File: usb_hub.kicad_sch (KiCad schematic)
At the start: 89 parts, among them J5 USB-C_WE_632723300011, J6 USB-C_WE_632723300011, U16 AP7366_SOT, U17 TPD4E05U06QDQARQ1, U18 AP22615A_TSOT26, U19 TPD4E05U06QDQARQ1, U20 AP22615A_TSOT26, U21 USB7252C, U22 W25Q80DV_USON, U24 TPD4E05U06QDQARQ1, U25 TPD4E05U06QDQARQ1, U27 TPD4E05U06QDQARQ1, U28 TPD4E05U06QDQARQ1, Y2 Oscillator_25MHz_ESC_2016MV

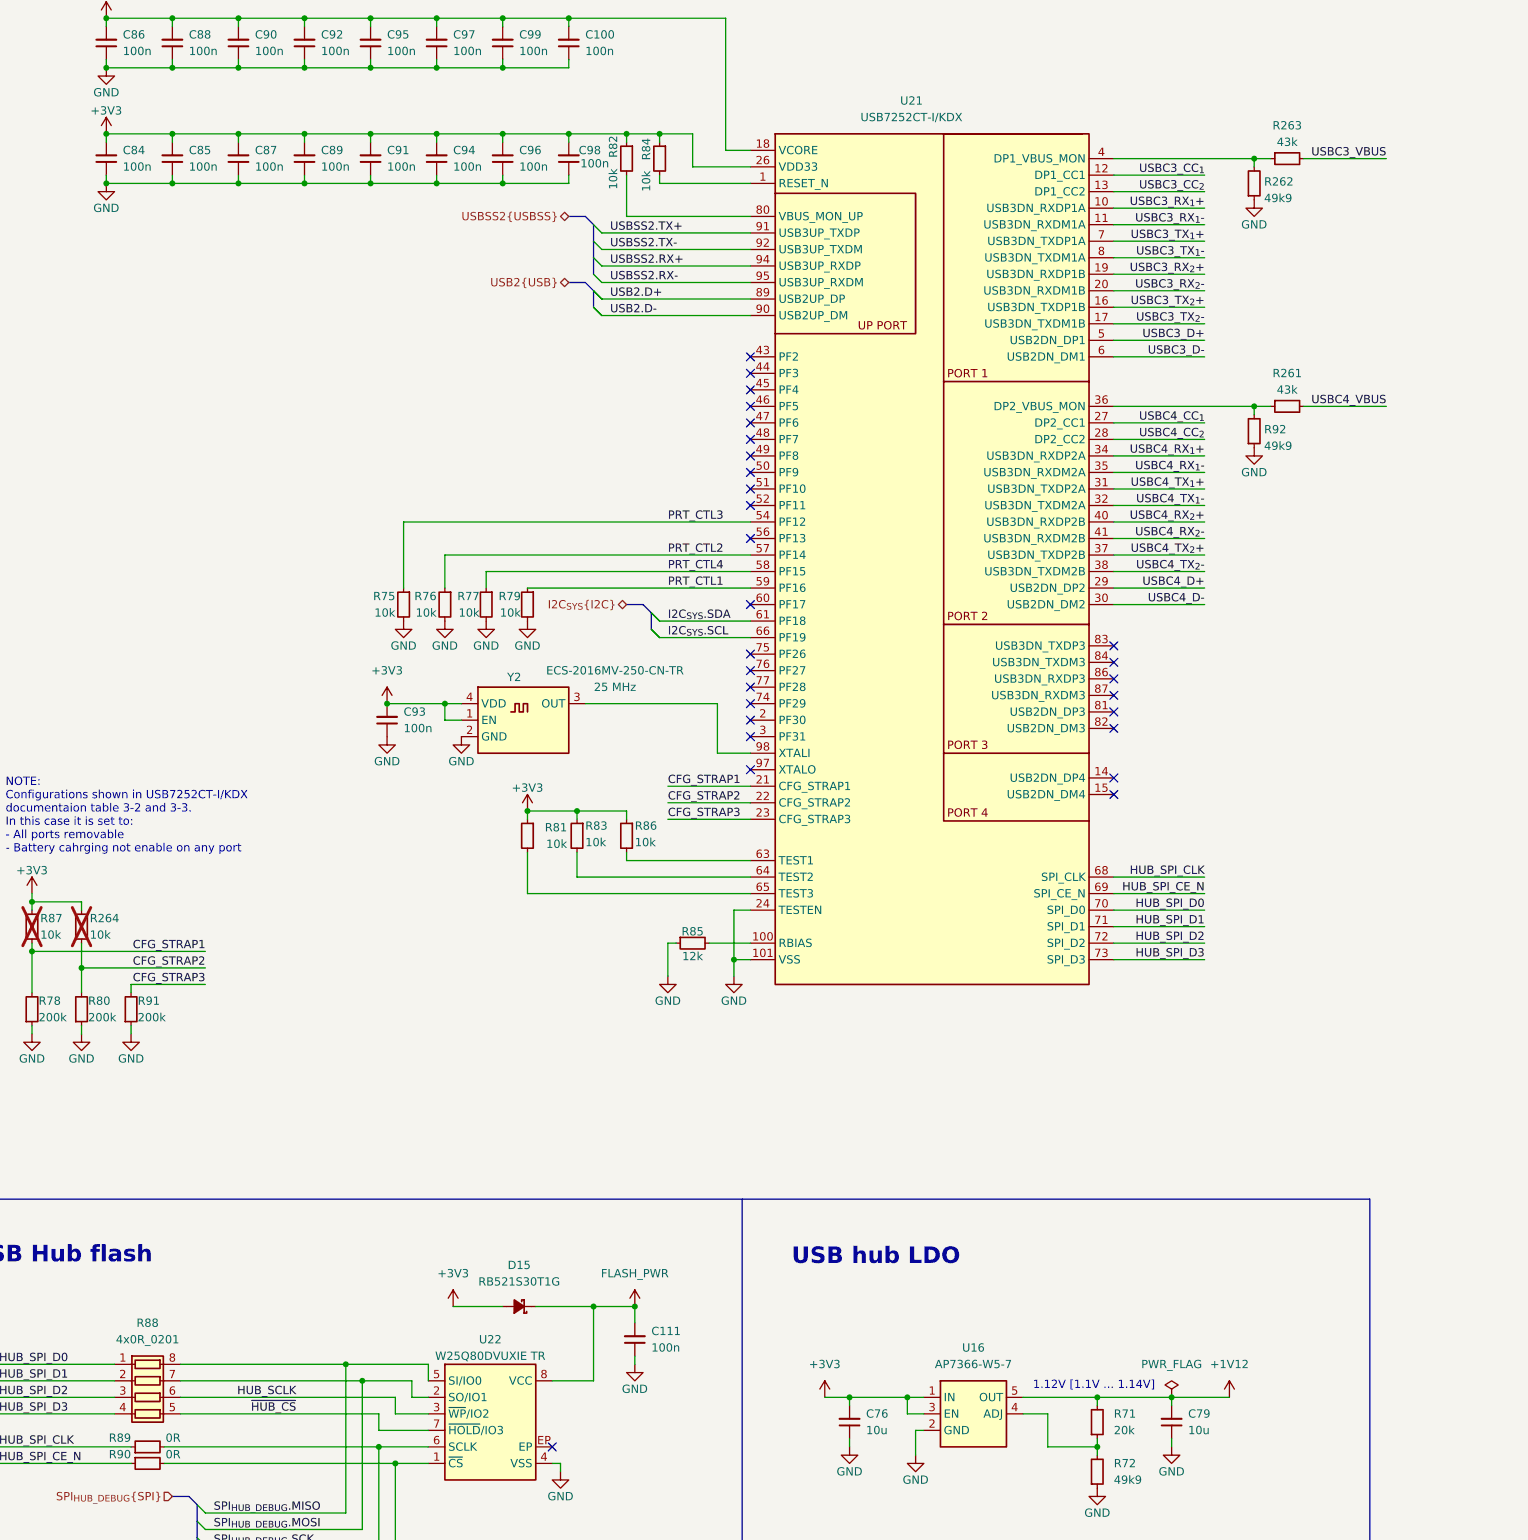
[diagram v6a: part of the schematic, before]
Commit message: [#83224] Schematic chages for easier USB hub routing
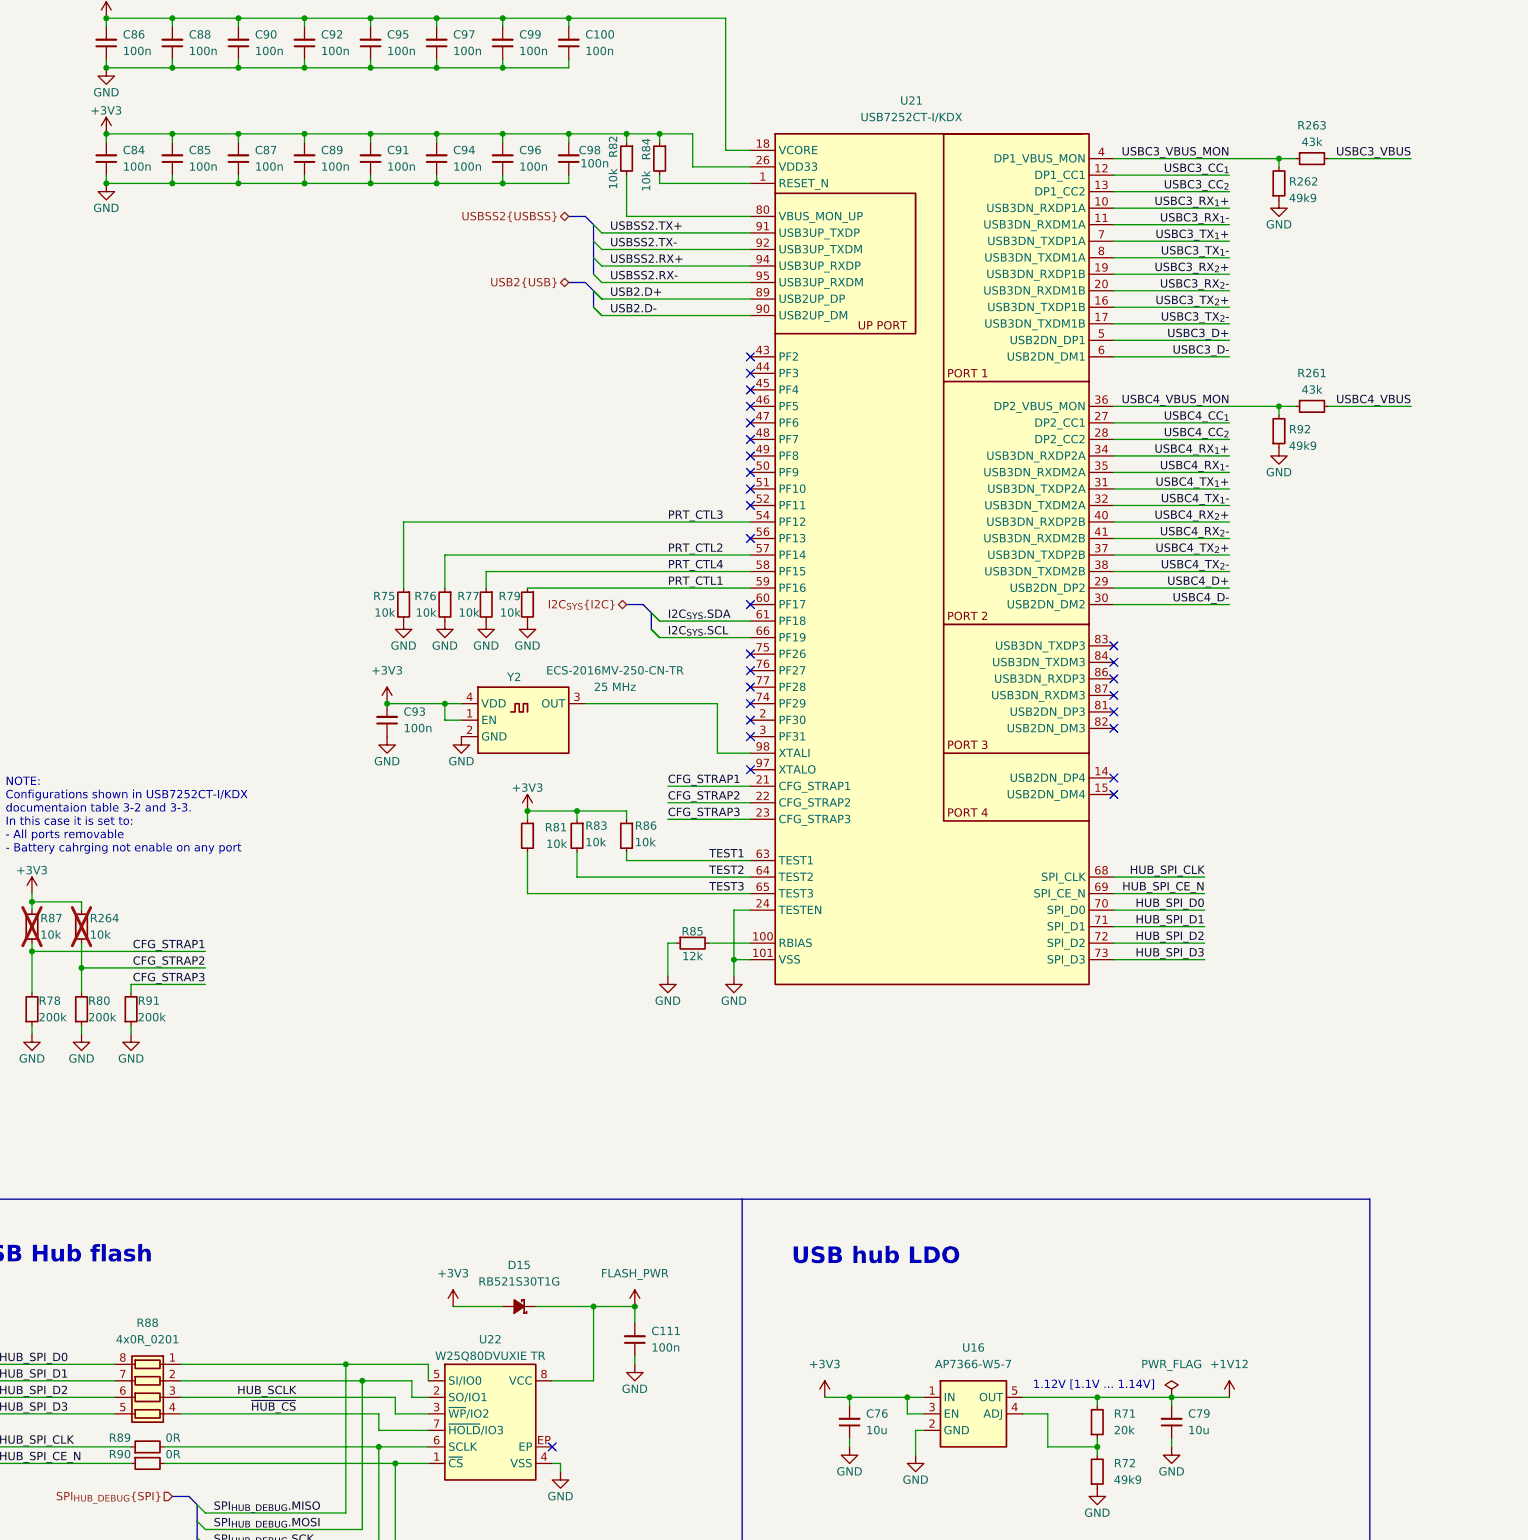
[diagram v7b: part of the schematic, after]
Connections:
- net HUB_SCLK: now also R88.3 (R3.1); no longer R88.6 (R3.2)
- net HUB_SPI_D0: now also R88.8 (R1.2); no longer R88.1 (R1.1)
- net HUB_SPI_D1: now also R88.7 (R2.2); no longer R88.2 (R2.1)
- net HUB_SPI_D2: now also R88.6 (R3.2); no longer R88.3 (R3.1)
- net HUB_SPI_D3: now also R88.5 (R4.2); no longer R88.4 (R4.1)
- net SPI_{HUB_DEBUG}.MISO: now also R88.1 (R1.1); no longer R88.8 (R1.2)
- net SPI_{HUB_DEBUG}.MOSI: now also R88.2 (R2.1); no longer R88.7 (R2.2)
- net ~{HUB_CS}: now also R88.4 (R4.1); no longer R88.5 (R4.2)
- net USBC4_VBUS_MON: now reaches R261.1, R92.2, U21.36 (DP2_VBUS_MON)
- net USBC3_VBUS_MON: now reaches R262.2, R263.1, U21.4 (DP1_VBUS_MON)
- net TEST1: now reaches R86.2, U21.63 (TEST1)
- net TEST2: now reaches R83.2, U21.64 (TEST2)
- net TEST3: now reaches R81.2, U21.65 (TEST3)
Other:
- moved on the sheet: R261, R262, R263, R92

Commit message: [#83224] Start placing USB
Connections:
- net USBC3_CC_{1}: now also U28.1, U28.10; no longer U28.5, U28.6
- net USBC3_CC_{2}: now also U28.5, U28.6; no longer U28.4, U28.7
- net USBC3_D+: now also J6.A7 (D_{A}-), J6.B7 (D_{B}-), U28.4, U28.7; no longer J6.A6 (D_{A}+), J6.B6 (D_{B}+), U28.2, U28.9
- net USBC3_D-: now also J6.A6 (D_{A}+), J6.B6 (D_{B}+), U28.2, U28.9; no longer J6.A7 (D_{A}-), J6.B7 (D_{B}-), U28.1, U28.10
- net USBC3_RX_{1}+: now also J6.B10 (RX_{1}-); no longer J6.B11 (RX_{1}+)
- net USBC3_RX_{1}-: now also J6.B11 (RX_{1}+); no longer J6.B10 (RX_{1}-)
- net USBC3_RX_{2}+: now also J6.A10 (RX_{2}-); no longer J6.A11 (RX_{2}+)
- net USBC3_RX_{2}-: now also J6.A11 (RX_{2}+); no longer J6.A10 (RX_{2}-)
- net USBC4_CC_{1}: now also U25.1, U25.10; no longer U25.5, U25.6
- net USBC4_CC_{2}: now also U25.5, U25.6; no longer U25.4, U25.7
- net USBC4_D+: now also J5.A7 (D_{A}-), J5.B7 (D_{B}-), U25.4, U25.7; no longer J5.A6 (D_{A}+), J5.B6 (D_{B}+), U25.2, U25.9
- net USBC4_D-: now also J5.A6 (D_{A}+), J5.B6 (D_{B}+), U25.2, U25.9; no longer J5.A7 (D_{A}-), J5.B7 (D_{B}-), U25.1, U25.10
- net USBC4_RX_{1}+: now also J5.B10 (RX_{1}-); no longer J5.B11 (RX_{1}+)
- net USBC4_RX_{1}-: now also J5.B11 (RX_{1}+); no longer J5.B10 (RX_{1}-)
- net USBC4_RX_{2}+: now also J5.A10 (RX_{2}-); no longer J5.A11 (RX_{2}+)
- net USBC4_RX_{2}-: now also J5.A11 (RX_{2}+); no longer J5.A10 (RX_{2}-)
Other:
- moved on the sheet: U28
